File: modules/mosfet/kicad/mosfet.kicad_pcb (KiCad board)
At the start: 2 copper layers, 9 parts, among them P1 CONN_01X02, P2 CONN_01X02, P3 CONN_01X02, P4 CONN_01X02, Q1 BC547, Q2 IRF540N

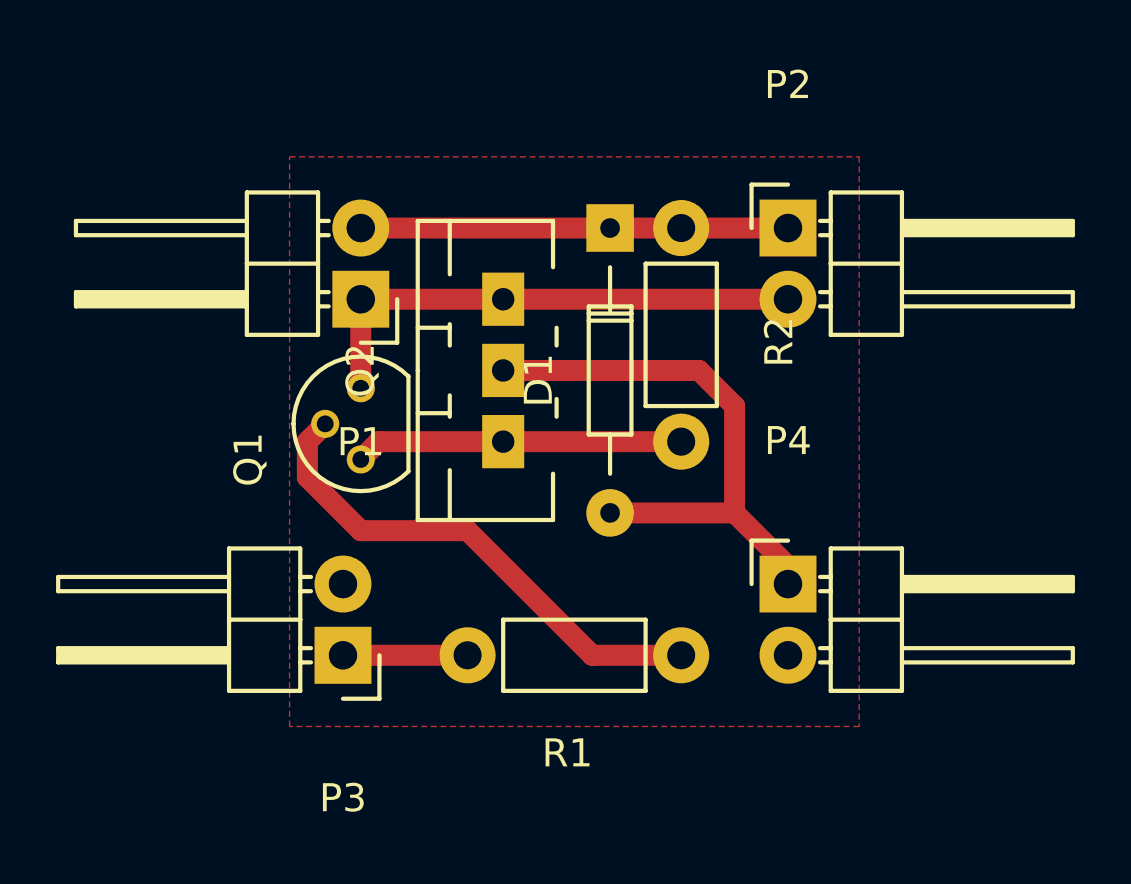
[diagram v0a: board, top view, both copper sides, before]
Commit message: Fixes issue #1
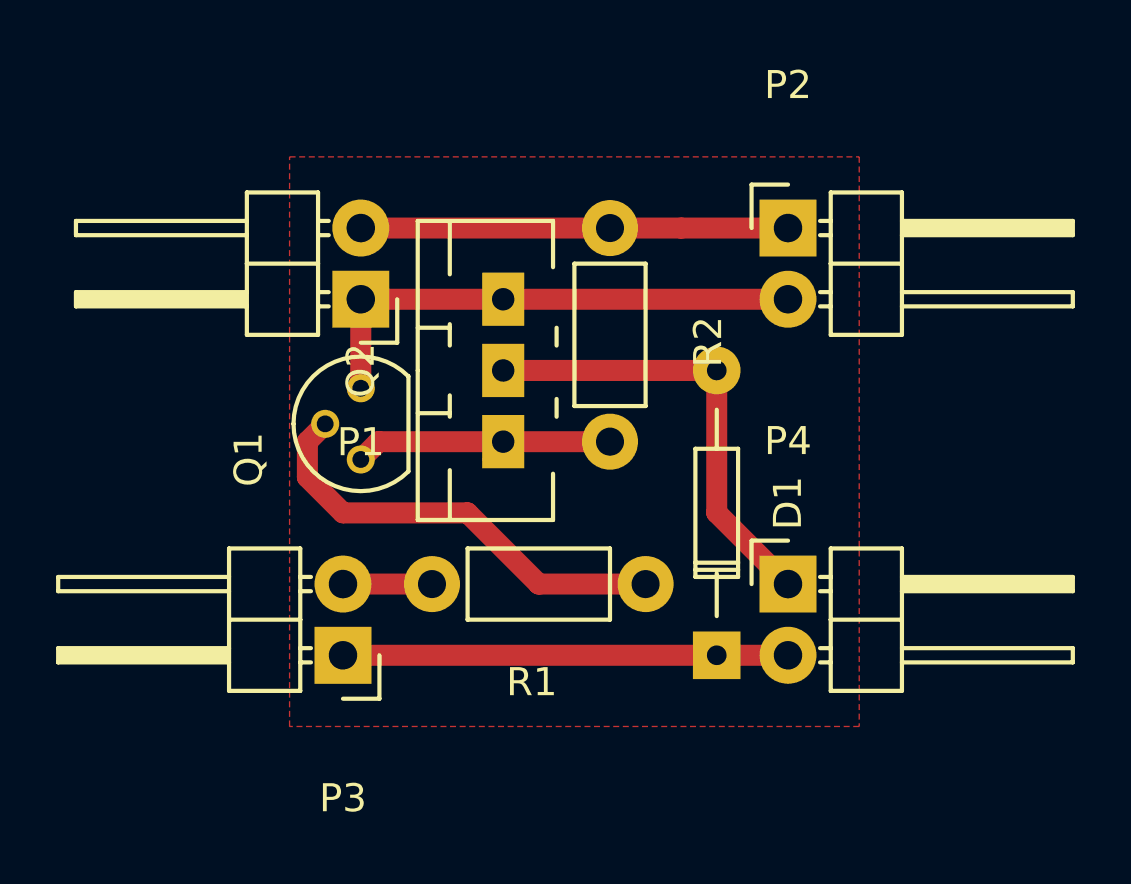
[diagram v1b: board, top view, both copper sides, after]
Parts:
- moved D1 15.7 mm to (130.8, 99.1), turned to 90 degrees
- moved R1 2.84 mm to (128.3, 96.5)
- moved R2 2.54 mm to (127.0, 83.8)
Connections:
- D1 pad 1: /VCC -> /VMOT
- P3 pad 1: /IN -> /VMOT
- P3 pad 2: Net-(P3-Pad2) -> /IN
- P4 pad 2: Net-(P4-Pad2) -> /VMOT
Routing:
- net /VMOT: track 0.00 -> 15.9 mm
- net /OUT: track 20.4 -> 16.9 mm
- net Net-(Q1-Pad1): track 12.6 -> 10.1 mm
- net Net-(Q1-Pad2): track 18.1 -> 15.8 mm
- net /IN: track 4.45 -> 3.18 mm
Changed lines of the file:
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@@
 (kicad_pcb (version 4) (host pcbnew 4.0.4+dfsg1-stable)
   (general
-    (links 12)
-    (no_connects 0)
-    (area 106.599999 77.745 144.225001 105.235)
+    (links 13)
+    (no_connects 1)
+    (area 0 0 0 0)
     (thickness 1.6)
     (drawings 4)
-    (tracks 26)
+    (tracks 24)
     (zones 0)
     (modules 9)
-    (nets 9)
+    (nets 8)
   )
   (page A4)
@@
     (last_trace_width 0.75)
     (trace_clearance 0.2)
-    (zone_clearance 1)
+    (zone_clearance 0.5)
     (zone_45_only no)
     (trace_min 0.2)
@@
   (net 5 "Net-(Q1-Pad1)")
   (net 6 /IN)
-  (net 7 "Net-(P3-Pad2)")
-  (net 8 "Net-(P4-Pad2)")
+  (net 7 /VMOT)
   (net_class Default "This is the default net class."
     (clearance 0.2)
@@
     (add_net /OUT)
     (add_net /VCC)
-    (add_net "Net-(P3-Pad2)")
-    (add_net "Net-(P4-Pad2)")
+    (add_net /VMOT)
     (add_net "Net-(Q1-Pad1)")
     (add_net "Net-(Q1-Pad2)")
@@
     (fp_line (start 1.524 -1.27) (end 1.524 1.27) (layer F.SilkS) (width 0.15))
     (pad 1 thru_hole rect (at 0 0 180) (size 2.032 2.032) (drill 1.016) (layers *.Cu *.Mask F.SilkS)
+      (net 7 /VMOT))
+    (pad 2 thru_hole oval (at 0 2.54 180) (size 2.032 2.032) (drill 1.016) (layers *.Cu *.Mask F.SilkS)
       (net 6 /IN))
-    (pad 2 thru_hole oval (at 0 2.54 180) (size 2.032 2.032) (drill 1.016) (layers *.Cu *.Mask F.SilkS)
-      (net 7 "Net-(P3-Pad2)"))
     (model Pin_Headers.3dshapes/Pin_Header_Angled_1x02.wrl
       (at (xyz 0 -0.05 0))
@@
       (net 2 /OUT))
     (pad 2 thru_hole oval (at 0 2.54) (size 2.032 2.032) (drill 1.016) (layers *.Cu *.Mask F.SilkS)
-      (net 8 "Net-(P4-Pad2)"))
+      (net 7 /VMOT))
     (model Pin_Headers.3dshapes/Pin_Header_Angled_1x02.wrl
       (at (xyz 0 -0.05 0))
@@
   )
   (module Resistors_ThroughHole:Resistor_Horizontal_RM7mm (layer F.Cu)
-    (at 129.54 99.06 180)
+    (at 128.27 96.52 180)
     (descr "Resistor, Axial,  RM 7.62mm, 1/3W,")
     (tags "Resistor Axial RM 7.62mm 1/3W R3")
@@
   )
   (module Resistors_ThroughHole:Resistor_Horizontal_RM7mm (layer F.Cu)
-    (at 129.54 83.82 270)
+    (at 127 83.82 270)
     (descr "Resistor, Axial,  RM 7.62mm, 1/3W,")
     (tags "Resistor Axial RM 7.62mm 1/3W R3")
@@
   )
   (module Diodes_ThroughHole:Diode_DO-35_SOD27_Horizontal_RM10 (layer F.Cu)
-    (at 127 83.82 270)
+    (at 130.81 99.06 90)
     (descr "Diode, DO-35,  SOD27, Horizontal, RM 10mm")
     (tags "Diode, DO-35, SOD27, Horizontal, RM 10mm, 1N4148,")
-    (fp_text reference D1 (at 5.43052 2.53746 270) (layer F.SilkS)
-      (effects (font (size 1 1) (thickness 0.15)))
-    )
-    (fp_text value D (at 4.41452 -3.55854 270) (layer F.Fab)
+    (fp_text reference D1 (at 5.43052 2.53746 90) (layer F.SilkS)
+      (effects (font (size 1 1) (thickness 0.15)))
+    )
+    (fp_text value D (at 4.41452 -3.55854 90) (layer F.Fab)
       (effects (font (size 1 1) (thickness 0.15)))
     )
@@
     (fp_line (start 7.36652 -0.76454) (end 2.79452 -0.76454) (layer F.SilkS) (width 0.15))
     (fp_line (start 2.79452 -0.76454) (end 2.79452 -0.00254) (layer F.SilkS) (width 0.15))
-    (pad 2 thru_hole circle (at 10.16052 -0.00254 90) (size 1.69926 1.69926) (drill 0.70104) (layers *.Cu *.Mask F.SilkS)
+    (pad 2 thru_hole circle (at 10.16052 -0.00254 270) (size 1.69926 1.69926) (drill 0.70104) (layers *.Cu *.Mask F.SilkS)
       (net 2 /OUT))
-    (pad 1 thru_hole rect (at 0.00052 -0.00254 90) (size 1.69926 1.69926) (drill 0.70104) (layers *.Cu *.Mask F.SilkS)
-      (net 1 /VCC))
+    (pad 1 thru_hole rect (at 0.00052 -0.00254 270) (size 1.69926 1.69926) (drill 0.70104) (layers *.Cu *.Mask F.SilkS)
+      (net 7 /VMOT))
     (model Diodes_ThroughHole.3dshapes/Diode_DO-35_SOD27_Horizontal_RM10.wrl
       (at (xyz 0.2 0 0))
@@
   (gr_line (start 135.89 101.6) (end 115.57 101.6) (angle 90) (layer Dwgs.User) (width 0.2))
   (segment (start 118.11 83.82) (end 127.00202 83.82) (width 0.75) (layer F.Cu) (net 1))
-  (segment (start 127.00202 83.82) (end 129.54 83.82) (width 0.75) (layer F.Cu) (net 1))
   (segment (start 129.54 83.82) (end 133.35 83.82) (width 0.75) (layer F.Cu) (net 1))
   (segment (start 133.34746 83.82254) (end 133.35 83.82) (width 0.25) (layer F.Cu) (net 1))
-  (segment (start 127.00254 93.98052) (end 131.44552 93.98052) (width 0.75) (layer F.Cu) (net 2))
-  (segment (start 131.44552 93.98052) (end 131.445 93.98) (width 0.75) (layer F.Cu) (net 2))
-  (segment (start 131.445 93.98) (end 131.445 90.17) (width 0.75) (layer F.Cu) (net 2))
-  (segment (start 131.445 90.17) (end 130.175 88.9) (width 0.75) (layer F.Cu) (net 2))
-  (segment (start 130.175 88.9) (end 123.19 88.9) (width 0.75) (layer F.Cu) (net 2))
+  (segment (start 127.00202 83.82) (end 129.54 83.82) (width 0.75) (layer F.Cu) (net 1))
+  (segment (start 130.80746 88.89948) (end 130.80746 93.97746) (width 0.75) (layer F.Cu) (net 2) (status 400000))
+  (segment (start 130.80746 93.97746) (end 133.35 96.52) (width 0.75) (layer F.Cu) (net 2) (status 800000))
+  (segment (start 130.80746 88.89948) (end 123.19052 88.89948) (width 0.75) (layer F.Cu) (net 2) (status C00000))
+  (segment (start 123.19052 88.89948) (end 123.19 88.9) (width 0.75) (layer F.Cu) (net 2) (status C00000))
   (segment (start 133.35 96.52) (end 133.35 95.885) (width 0.25) (layer F.Cu) (net 2))
-  (segment (start 133.35 95.885) (end 131.445 93.98) (width 0.75) (layer F.Cu) (net 2))
-  (segment (start 127.00306 93.98) (end 127.00254 93.98052) (width 0.25) (layer F.Cu) (net 2))
   (segment (start 133.35 86.36) (end 123.19 86.36) (width 0.75) (layer F.Cu) (net 3))
   (segment (start 123.19 86.36) (end 118.11 86.36) (width 0.75) (layer F.Cu) (net 3))
   (segment (start 118.11 86.36) (end 118.11 89.535) (width 0.75) (layer F.Cu) (net 3))
-  (segment (start 116.84 90.805) (end 116.205 91.44) (width 0.75) (layer F.Cu) (net 4) (status 400000))
-  (segment (start 126.365 99.06) (end 129.54 99.06) (width 0.75) (layer F.Cu) (net 4) (status 800000))
-  (segment (start 121.92 94.615) (end 126.365 99.06) (width 0.75) (layer F.Cu) (net 4))
-  (segment (start 118.11 94.615) (end 121.92 94.615) (width 0.75) (layer F.Cu) (net 4))
-  (segment (start 116.205 92.71) (end 118.11 94.615) (width 0.75) (layer F.Cu) (net 4))
-  (segment (start 116.205 91.44) (end 116.205 92.71) (width 0.75) (layer F.Cu) (net 4))
+  (segment (start 128.27 96.52) (end 124.46 96.52) (width 0.75) (layer F.Cu) (net 4))
+  (segment (start 116.205 91.44) (end 116.84 90.805) (width 0.75) (layer F.Cu) (net 4))
+  (segment (start 116.205 92.71) (end 116.205 91.44) (width 0.75) (layer F.Cu) (net 4))
+  (segment (start 117.475 93.98) (end 116.205 92.71) (width 0.75) (layer F.Cu) (net 4))
+  (segment (start 121.92 93.98) (end 117.475 93.98) (width 0.75) (layer F.Cu) (net 4))
+  (segment (start 124.46 96.52) (end 121.92 93.98) (width 0.75) (layer F.Cu) (net 4))
+  (segment (start 123.19 91.44) (end 127 91.44) (width 0.75) (layer F.Cu) (net 5) (status C00000))
   (segment (start 123.19 91.44) (end 118.745 91.44) (width 0.75) (layer F.Cu) (net 5))
   (segment (start 118.745 91.44) (end 118.11 92.075) (width 0.75) (layer F.Cu) (net 5))
-  (segment (start 123.19 91.44) (end 129.54 91.44) (width 0.75) (layer F.Cu) (net 5))
   (segment (start 122.555 92.075) (end 123.19 91.44) (width 0.25) (layer F.Cu) (net 5))
-  (segment (start 117.475 99.06) (end 121.92 99.06) (width 0.75) (layer F.Cu) (net 6))
+  (segment (start 120.65 96.52) (end 117.475 96.52) (width 0.75) (layer F.Cu) (net 6))
+  (segment (start 133.35 99.06) (end 117.475 99.06) (width 0.75) (layer F.Cu) (net 7))
   (zone (net 0) (net_name "") (layer F.Cu) (hatch edge 0.508)
-    (connect_pads yes (clearance 1))
-    (min_thickness 0.7)
+    (connect_pads yes (clearance 0.5))
+    (min_thickness 0.4)
     (fill yes (arc_segments 16) (thermal_gap 0.8) (thermal_bridge_width 0.5))
     (polygon
